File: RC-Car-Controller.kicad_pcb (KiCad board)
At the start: 4 copper layers, 104 x 74 mm, 104 parts, among them J1 USB_C_Receptacle_USB2.0, J2 Power_Input, J3 Conn_01x11_Socket, J4 MOTOR_1_OUTPUT, J5 MOTOR_2_OUTPUT, J6 MOTOR_3_OUTPUT, J7 MOTOR_4_OUTPUT, J8 Conn_01x03_Socket, J9 Conn_01x11_Socket, SW2 SW_Push, SW4 SW_Push, U1 LMR14020SDDAR, U10 DRV8874PWPR, U11 DRV8874PWPR, U2 SPX3819M5-L-3-3, U3 USBLC6-2SC6, U5 DRV8874PWPR, U6 W25Q32JVSS, U8 ESP32-S3, U9 DRV8874PWPR, X2 40MHz

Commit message: checkpoint for backup
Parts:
- added JP1: Jumper_PMODE, Connector_PinHeader_2.54mm:PinHeader_1x03_P2.54mm_Vertical_SMD_Pin1Right, F.Cu at (148.4, 72.4)
- added R19: 16K, Resistor_SMD:R_0603_1608Metric, F.Cu at (62.9, 79.7)
- added R20: 50K, Resistor_SMD:R_0603_1608Metric, F.Cu at (62.9, 77.8)
- added R4: 16K, Resistor_SMD:R_0603_1608Metric, F.Cu at (79.3, 79.7)
- added R7: 50K, Resistor_SMD:R_0603_1608Metric, F.Cu at (79.3, 78.0)
- moved J3 125.6 mm to (149.9, 47.7)
- moved R16 59.2 mm to (63.3, 75.4)
- moved R13 43.3 mm to (79.6, 75.2)
- moved R15 40.4 mm to (116.8, 78.8), turned to 0 degrees
- moved R14 37.5 mm to (116.8, 81.0)
- moved C14 34.2 mm to (82.0, 58.8), turned to 0 degrees
- moved J1 31.2 mm to (73.0, 23.9), turned to 180 degrees
- moved C13 27.6 mm to (78.7, 63.1)
- moved J8 26.9 mm to (101.1, 49.3), turned to 0 degrees
- moved J7 26.4 mm to (63.9, 87.1), turned to 0 degrees
- moved J4 26.0 mm to (118.0, 86.8), turned to 0 degrees
- moved C12 24.5 mm to (78.7, 65.1), turned to 180 degrees
- moved C42 24.2 mm to (116.2, 64.1), turned to 180 degrees
- moved C11 24.0 mm to (76.2, 65.1), turned to 0 degrees
- moved J6 23.5 mm to (80.4, 86.9), turned to 0 degrees
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- renumbered IMU to IMU1, MGN to MGN1
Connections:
- C45 pad 1: /Sensors/VDD_IO -> +3V3
- J2 pad 1: GND -> +36V
- J2 pad 2: +36V -> GND
- J3 pad 10: GPIO10 -> unconnected-(J3-Pin_10-Pad10)
- J3 pad 11: GPIO11 -> unconnected-(J3-Pin_11-Pad11)
- J3 pad 7: GPIO7 -> unconnected-(J3-Pin_7-Pad7)
- J3 pad 8: GPIO8 -> unconnected-(J3-Pin_8-Pad8)
- J3 pad 9: GPIO9 -> unconnected-(J3-Pin_9-Pad9)
- J9 pad 1: GPIO12 -> unconnected-(J9-Pin_1-Pad1)
- J9 pad 2: GPIO13 -> unconnected-(J9-Pin_2-Pad2)
- J9 pad 4: GPIO15 -> GPIO17
- J9 pad 5: GPIO16 -> GPIO18
- MGN1 pad 10: /Sensors/VDD_IO -> +3V3
- MGN1 pad 7: MGN_DRDY -> GND
- R14 pad 2: /Motors/PROP_VREF -> /Motors/PROP_VREF_1
- R15 pad 1: /Motors/PROP_VREF -> /Motors/PROP_VREF_1
- R5 pad 2: /Motors/PROP_VREF -> /Motors/PROP_VREF_2
- R6 pad 1: /Motors/PROP_VREF -> /Motors/PROP_VREF_2
- U10 pad 16: MOTOR_1_PMODE -> MOTOR_PMODE
- U10 pad 17: (no net) -> GND
- U10 pad 4: MOTOR_1_NFAULT -> MOTOR_NFAULT
- U10 pad 5: /Motors/PROP_VREF -> /Motors/PROP_VREF_1
- U11 pad 16: MOTOR_4_PMODE -> MOTOR_PMODE
- U11 pad 17: (no net) -> GND
- U11 pad 4: MOTOR_4_NFAULT -> MOTOR_NFAULT
- U11 pad 5: /Motors/PROP_VREF -> /Motors/PROP_VREF_4
- U5 pad 16: MOTOR_3_PMODE -> MOTOR_PMODE
- U5 pad 17: (no net) -> GND
- U5 pad 4: MOTOR_3_NFAULT -> MOTOR_NFAULT
- U5 pad 5: /Motors/PROP_VREF -> /Motors/PROP_VREF_3
- U8 pad 27: unconnected-(U8-GPIO21-Pad27) -> MOTOR_NFAULT
- U8 pad 28: unconnected-(U8-SPI_CS1/GPIO26-Pad28) -> GPIO26
- U8 pad 51: unconnected-(U8-GPIO45-Pad51) -> GPIO45
- U8 pad 52: unconnected-(U8-GPIO46-Pad52) -> GPIO46
- U9 pad 16: MOTOR_2_PMODE -> MOTOR_PMODE
- U9 pad 17: (no net) -> GND
- U9 pad 4: MOTOR_2_NFAULT -> MOTOR_NFAULT
- U9 pad 5: /Motors/PROP_VREF -> /Motors/PROP_VREF_2
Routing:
- net MOTOR_PMODE: track 0.00 -> 104.2 mm, vias 0 -> 5
- net MOTOR_4_OUT_2: track 0.00 -> 24.5 mm
- net MOTOR_1_OUT_2: track 0.00 -> 24.5 mm
- net MOTOR_3_OUT_2: track 0.00 -> 24.5 mm
- net +3V3: track 51.2 -> 72.8 mm, vias 18 -> 26
- net +36V: track 27.3 -> 45.8 mm, vias 12 -> 16
- net MOTOR_NFAULT: track 0.00 -> 17.2 mm, vias 0 -> 4
- net MOTOR_3_OUT_1: track 0.00 -> 15.8 mm
- net MOTOR_4_OUT_1: track 0.00 -> 15.8 mm
- net MOTOR_1_OUT_1: track 0.00 -> 15.6 mm
- net +VBUS: track 29.1 -> 13.9 mm
- net GND: track 90.5 -> 102.5 mm, vias 76 -> 98
- net +5V: track 20.3 -> 29.3 mm
- net MOTOR_2_OUT_2: track 17.8 -> 25.1 mm
- net /Motors/PROP_VREF_1: track 0.00 -> 7.18 mm
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- removed copper zone on B.Cu, net +36V
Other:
- board size 104 x 74 mm -> 107 x 77.9 mm

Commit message: Checkpoint before updating MCU
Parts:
- added C10: 100n, Capacitor_SMD:C_0402_1005Metric, F.Cu at (-87.1, 67.5)
- added C53: 1u, Capacitor_SMD:C_0402_1005Metric, F.Cu at (-87.1, 69.4)
- added C54: 100n, Capacitor_SMD:C_0402_1005Metric, F.Cu at (-87.1, 71.4)
- added C55: 12p, Capacitor_SMD:C_0402_1005Metric, F.Cu at (-87.1, 73.4)
- added C56: 12p, Capacitor_SMD:C_0402_1005Metric, F.Cu at (-87.1, 75.3)
- added C9: 100n, Capacitor_SMD:C_0402_1005Metric, F.Cu at (-87.1, 65.5)
- added R22: 5k1, Resistor_SMD:R_0603_1608Metric, F.Cu at (-75.2, 80.8)
- added SW1: SW_Push, Button_Switch_SMD:SW_Push_SPST_NO_Alps_SKRK, F.Cu at (-85.7, 81.7)
- added U4: ESP32-S3-WROOM-1, RF_Module:ESP32-S3-WROOM-1, F.Cu at (-48.9, 55.9)
- added X3: 32.768Khz, Crystal:Crystal_SMD_3225-4Pin_3.2x2.5mm, F.Cu at (-79.8, 81.7)
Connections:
- U10 pad 17: GND -> (no net)
- U11 pad 17: GND -> (no net)
- U5 pad 17: GND -> (no net)
- U9 pad 17: GND -> (no net)

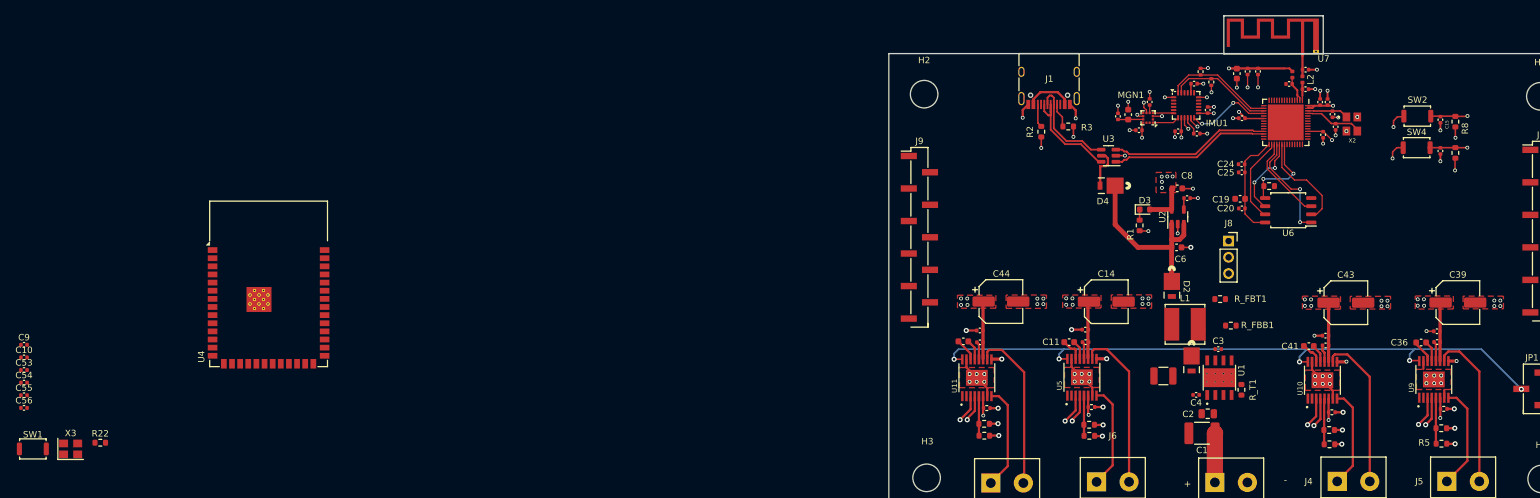
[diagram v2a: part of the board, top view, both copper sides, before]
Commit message: Replace MCU with WROOM-1 unit + route
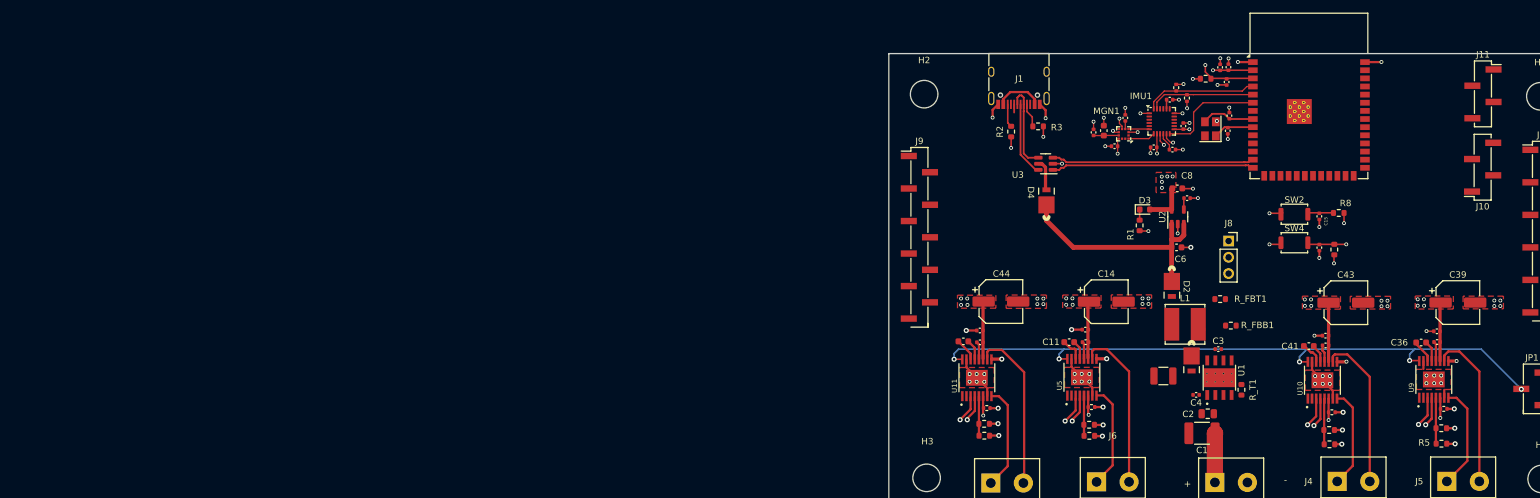
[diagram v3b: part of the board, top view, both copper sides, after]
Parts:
- removed C20, C24, C29, C30, C31, C32, C54: 100n, Capacitor_SMD:C_0402_1005Metric
- removed C21, C22: 3p3, Capacitor_SMD:C_0402_1005Metric
- removed C23, C26: 20p, Capacitor_SMD:C_0402_1005Metric
- removed C25, C28, C53: 1u, Capacitor_SMD:C_0402_1005Metric
- removed C27: 10u, Capacitor_SMD:C_0603_1608Metric
- removed C33: 10nF, Capacitor_SMD:C_0402_1005Metric
- removed C34: 1uF, Capacitor_SMD:C_0402_1005Metric
- removed L2, L3: 2n2, Inductor_SMD:L_0402_1005Metric
- removed R22: 5k1, Resistor_SMD:R_0603_1608Metric
- removed SW1: SW_Push, Button_Switch_SMD:SW_Push_SPST_NO_Alps_SKRK
- removed U6: W25Q32JVSS, Package_SO:SOIC-8_5.23x5.23mm_P1.27mm
- removed U7: ~, RF_Antenna:Texas_SWRA117D_2.4GHz_Left
- removed U8: ESP32-S3, Package_DFN_QFN:QFN-56-1EP_7x7mm_P0.4mm_EP5.6x5.6mm
- removed X2: 40MHz, KiCADv7:OSC_X322516MLB4SI
- added J10: JTAG, Connector_PinHeader_2.54mm:PinHeader_1x04_P2.54mm_Vertical_SMD_Pin1Right, F.Cu at (140.7, 37.7)
- added J11: UART, Connector_PinHeader_2.54mm:PinHeader_1x04_P2.54mm_Vertical_SMD_Pin1Right, F.Cu at (140.8, 26.3)
- C19: value 10u -> 100n; footprint Capacitor_SMD:C_0603_1608Metric -> Capacitor_SMD:C_0402_1005Metric
- C9: value 100n -> 22u
- X3: value 32.768Khz -> 32.768KHz
- moved C55 193.3 mm to (101.2, 29.7), turned to 90 degrees
- moved C9 193.0 mm to (101.0, 22.1), turned to 90 degrees
- moved C56 192.9 mm to (100.9, 32.1), turned to -90 degrees
- moved C10 192.2 mm to (99.7, 22.1), turned to 90 degrees
- moved X3 184.9 mm to (98.2, 31.8), turned to 90 degrees
- moved U4 165.1 mm to (113.6, 26.6)
- moved SW2 24.6 mm to (111.3, 45.1)
- moved R10 24.2 mm to (117.6, 50.6)
- moved C15 24.2 mm to (115.2, 45.4)
- moved C16 24.2 mm to (115.2, 50.3)
- moved SW4 24.2 mm to (111.3, 49.5)
- moved R8 23.1 mm to (118.3, 44.9), turned to 180 degrees
- moved R12 19.5 mm to (97.5, 23.9)
- moved C19 18.4 mm to (100.8, 24.4), turned to -90 degrees
- moved D4 10.3 mm to (72.6, 42.9), turned to 90 degrees
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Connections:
- net /ESP32-S3 Microcontroller /RESET renamed Net-(C15-Pad1)
- C16 pad 1: /ESP32-S3 Microcontroller /CHIP_BOOT -> /ESP32-S3 Microcontroller /BOOT
- C19 pad 1: /ESP32-S3 Microcontroller /VDD_SPI -> /ESP32-S3 Microcontroller /ENABLE
- R10 pad 2: /ESP32-S3 Microcontroller /CHIP_BOOT -> /ESP32-S3 Microcontroller /BOOT
- R12 pad 1: /ESP32-S3 Microcontroller /SPID -> +3V3
- R12 pad 2: +3V3 -> /ESP32-S3 Microcontroller /ENABLE
- R8 pad 1: +3V3 -> /ESP32-S3 Microcontroller /ENABLE
- SW4 pad 2: /ESP32-S3 Microcontroller /CHIP_BOOT -> /ESP32-S3 Microcontroller /BOOT
- U4 pad 32: unconnected-(U4-IO39-Pad32) -> TCK
- U4 pad 33: unconnected-(U4-IO40-Pad33) -> TDO
- U4 pad 34: unconnected-(U4-IO41-Pad34) -> TDI
- U4 pad 35: unconnected-(U4-IO42-Pad35) -> TMS
- U4 pad 36: unconnected-(U4-RXD0-Pad36) -> GPIO44_RX
- U4 pad 37: unconnected-(U4-TXD0-Pad37) -> GPIO43_TX
- U4 pad 4: unconnected-(U4-IO4-Pad4) -> SDA
- U4 pad 5: unconnected-(U4-IO5-Pad5) -> SCL
- U4 pad 6: unconnected-(U4-IO6-Pad6) -> INT_IMU
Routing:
- net +3V3: track 72.8 -> 53.9 mm, vias 26 -> 23
- net /ESP32-S3 Microcontroller /SPICSO: track 17.1 -> 0.00 mm, vias 2 -> 0
- net /ESP32-S3 Microcontroller /VDD_SPI: track 16.8 -> 0.00 mm
- net /ESP32-S3 Microcontroller /SPIQ: track 15.8 -> 0.00 mm
- net /ESP32-S3 Microcontroller /SPIWP: track 13.6 -> 0.00 mm
- net /ESP32-S3 Microcontroller /SPIHD: track 13.4 -> 0.00 mm
- net /ESP32-S3 Microcontroller /SPID: track 13.3 -> 0.00 mm, vias 2 -> 0
- net /ESP32-S3 Microcontroller /SPICLK: track 12.6 -> 0.00 mm, vias 2 -> 0
- net /ESP32-S3 Microcontroller /ENABLE: track 0.00 -> 10.5 mm, vias 0 -> 2
- net Net-(U8-XTAL_N): track 9.02 -> 0.00 mm
- net /ESP32-S3 Microcontroller /XTAL_P: track 0.00 -> 8.40 mm
- net +5V: track 29.3 -> 36.6 mm
- net USB_D_P: track 25.0 -> 31.7 mm
- net USB_D_N: track 25.0 -> 31.7 mm
- net Net-(U8-XTAL_P): track 6.43 -> 0.00 mm
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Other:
- board size 107 x 77.9 mm -> 107 x 72 mm

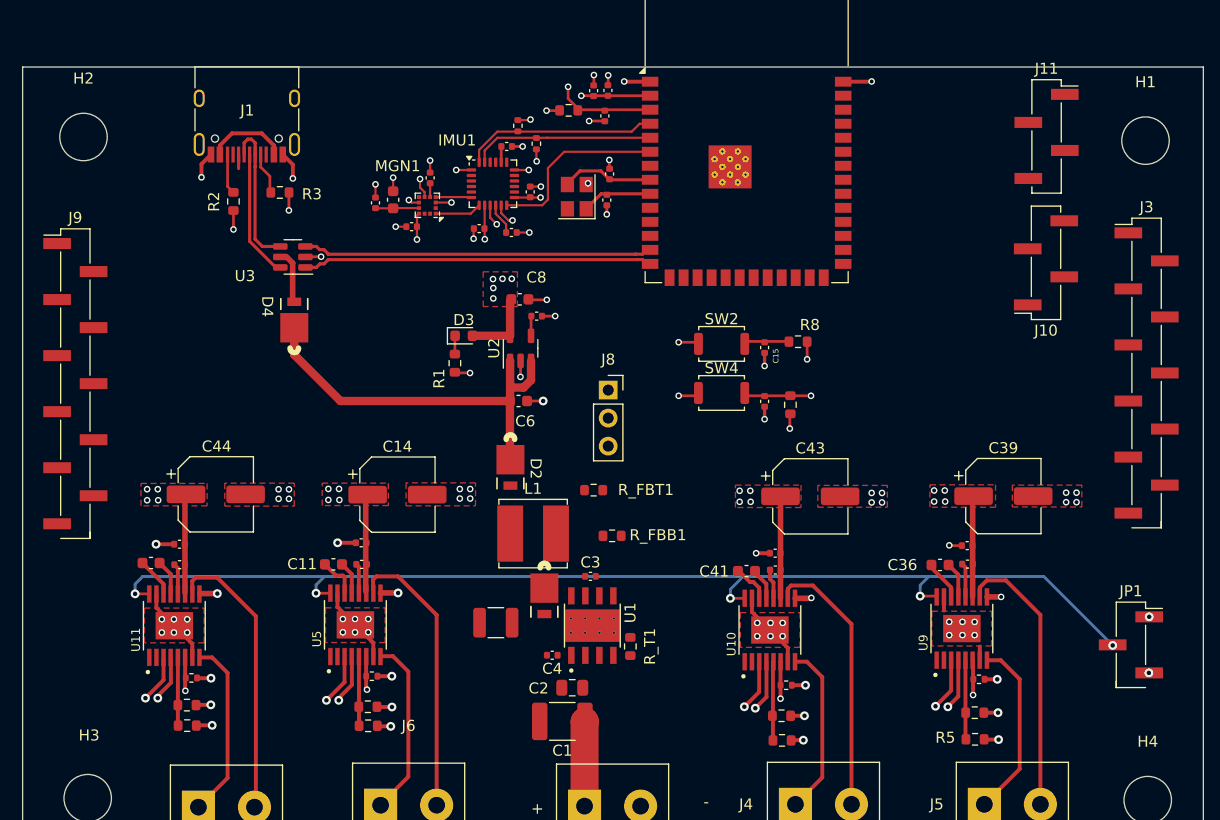
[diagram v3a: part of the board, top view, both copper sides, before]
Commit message: Route Motor Drivers
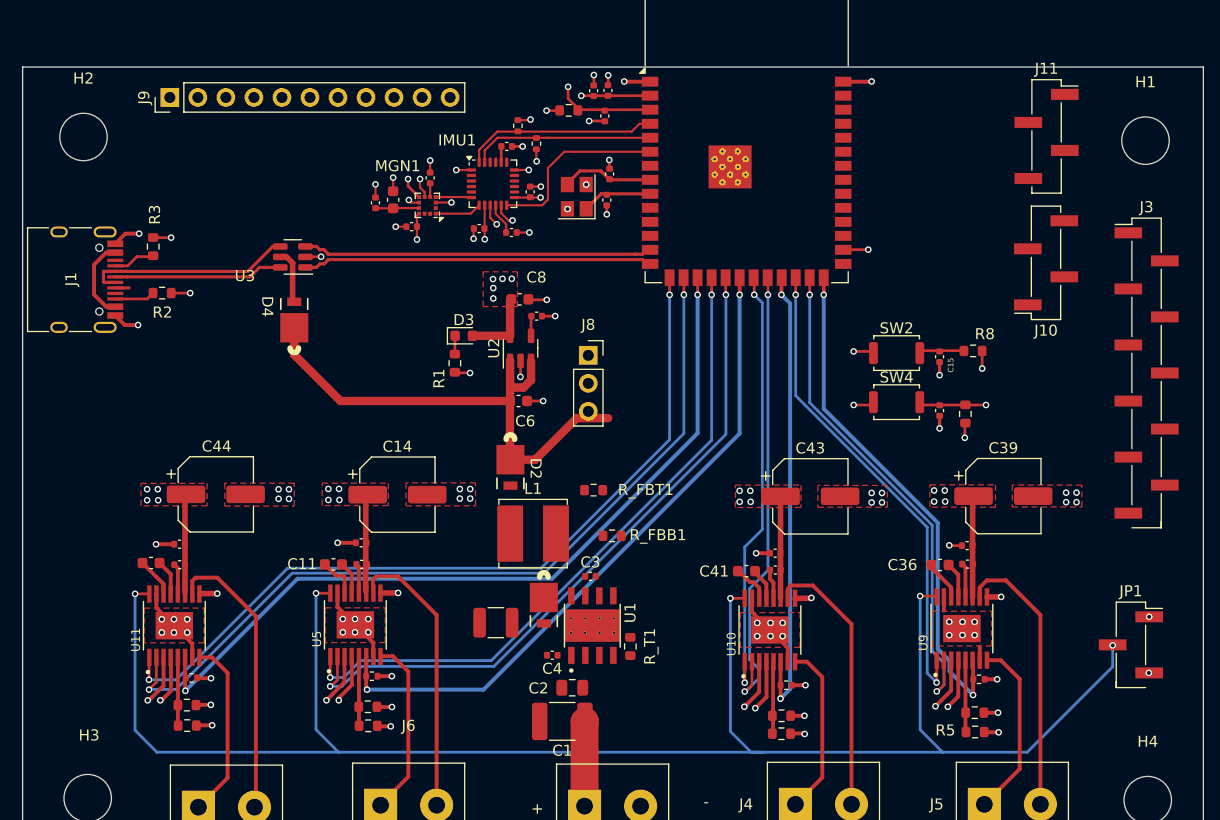
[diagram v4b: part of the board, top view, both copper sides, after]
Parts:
- J9: footprint Connector_PinHeader_2.54mm:PinHeader_1x11_P2.54mm_Vertical_SMD_Pin1Left -> Connector_PinHeader_2.54mm:PinHeader_1x11_P2.54mm_Vertical
- moved J9 27.3 mm to (61.3, 22.8), turned to 90 degrees
- moved J1 22.2 mm to (52.3, 39.3), turned to -90 degrees
- moved R10 15.9 mm to (133.4, 51.4)
- moved C15 15.9 mm to (131.1, 46.3)
- moved C16 15.9 mm to (131.1, 51.1)
- moved R8 15.9 mm to (134.1, 45.7)
- moved SW2 15.9 mm to (127.2, 45.9)
- moved SW4 15.9 mm to (127.2, 50.4)
- moved R3 12.5 mm to (59.8, 36.3), turned to 90 degrees
- moved R2 10.5 mm to (60.6, 40.5), turned to 0 degrees
- moved J8 3.63 mm to (99.3, 46.1)
- moved D1 0.85 mm to (95.2, 68.8)
- moved R5 0.66 mm to (134.3, 80.3)
- moved R14 0.61 mm to (116.8, 80.4)
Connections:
- J4 pad 1: MOTOR_1_OUT_1 -> MOTOR_2_OUT_1
- J4 pad 2: MOTOR_1_OUT_2 -> MOTOR_2_OUT_2
- J5 pad 1: MOTOR_2_OUT_1 -> MOTOR_1_OUT_1
- J5 pad 2: MOTOR_2_OUT_2 -> MOTOR_1_OUT_2
- R11 pad 1: MOTOR_1_PROP -> MOTOR_2_PROP
- R9 pad 1: MOTOR_2_PROP -> MOTOR_1_PROP
- U10 pad 1: MOTOR_1_PWM -> MOTOR_2_PWM
- U10 pad 10: MOTOR_1_OUT_2 -> MOTOR_2_OUT_2
- U10 pad 2: MOTOR_1_DIRECTION -> MOTOR_2_DIRECTION
- U10 pad 6: MOTOR_1_PROP -> MOTOR_2_PROP
- U10 pad 8: MOTOR_1_OUT_1 -> MOTOR_2_OUT_1
- U4 pad 15: unconnected-(U4-IO3-Pad15) -> MOTOR_4_PWM
- U4 pad 16: unconnected-(U4-IO46-Pad16) -> MOTOR_4_DIRECTION
- U4 pad 17: unconnected-(U4-IO9-Pad17) -> MOTOR_4_PROP
- U4 pad 18: unconnected-(U4-IO10-Pad18) -> MOTOR_3_PWM
- U4 pad 19: unconnected-(U4-IO11-Pad19) -> MOTOR_3_DIRECTION
- U4 pad 20: unconnected-(U4-IO12-Pad20) -> MOTOR_3_PROP
- U4 pad 21: unconnected-(U4-IO13-Pad21) -> MOTOR_2_PWM
- U4 pad 22: unconnected-(U4-IO14-Pad22) -> MOTOR_2_DIRECTION
- U4 pad 23: unconnected-(U4-IO21-Pad23) -> MOTOR_2_PROP
- U4 pad 24: unconnected-(U4-IO47-Pad24) -> MOTOR_1_PWM
- U4 pad 25: unconnected-(U4-IO48-Pad25) -> MOTOR_1_DIRECTION
- U4 pad 26: unconnected-(U4-IO45-Pad26) -> MOTOR_1_PROP
- U4 pad 28: unconnected-(U4-IO35-Pad28) -> MOTOR_NFAULT
- U9 pad 1: MOTOR_2_PWM -> MOTOR_1_PWM
- U9 pad 10: MOTOR_2_OUT_2 -> MOTOR_1_OUT_2
- U9 pad 2: MOTOR_2_DIRECTION -> MOTOR_1_DIRECTION
- U9 pad 6: MOTOR_2_PROP -> MOTOR_1_PROP
- U9 pad 8: MOTOR_2_OUT_1 -> MOTOR_1_OUT_1
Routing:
- net MOTOR_NFAULT: track 17.2 -> 150.1 mm, vias 4 -> 5
- net MOTOR_4_DIRECTION: track 0.00 -> 75.5 mm, vias 0 -> 2
- net MOTOR_4_PWM: track 0.00 -> 72.9 mm, vias 0 -> 2
- net MOTOR_4_PROP: track 3.04 -> 73.2 mm, vias 1 -> 2
- net MOTOR_3_DIRECTION: track 0.00 -> 62.6 mm, vias 0 -> 2
- net MOTOR_3_PWM: track 0.00 -> 60.1 mm, vias 0 -> 2
- net MOTOR_3_PROP: track 3.04 -> 60.5 mm, vias 1 -> 2
- net MOTOR_PMODE: track 104.2 -> 158.4 mm
- net MOTOR_1_DIRECTION: track 0.00 -> 46.0 mm, vias 0 -> 2
- net MOTOR_1_PWM: track 0.00 -> 44.0 mm, vias 0 -> 2
- net MOTOR_1_PROP: track 3.38 -> 46.7 mm, vias 1 -> 2
- net MOTOR_2_DIRECTION: track 0.00 -> 42.1 mm, vias 0 -> 2
- net MOTOR_2_PWM: track 0.00 -> 39.8 mm, vias 0 -> 2
- net MOTOR_2_PROP: track 3.26 -> 42.2 mm, vias 1 -> 2
- net +5V: track 36.6 -> 47.0 mm
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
